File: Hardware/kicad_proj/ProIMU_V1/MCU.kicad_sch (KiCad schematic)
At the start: 8 parts, among them U9 STM32F412CEU6

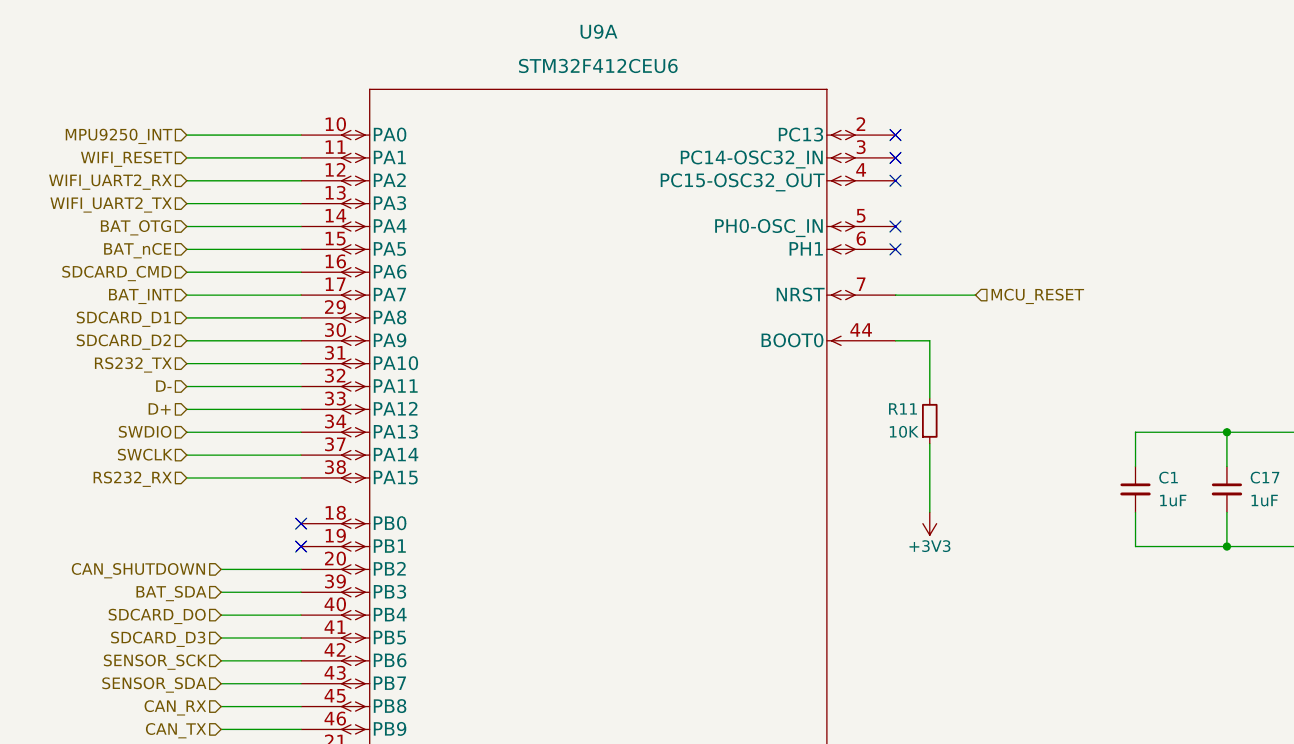
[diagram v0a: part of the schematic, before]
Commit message: Updated Schematic and Layout. Connectors and SD Card Port changed.
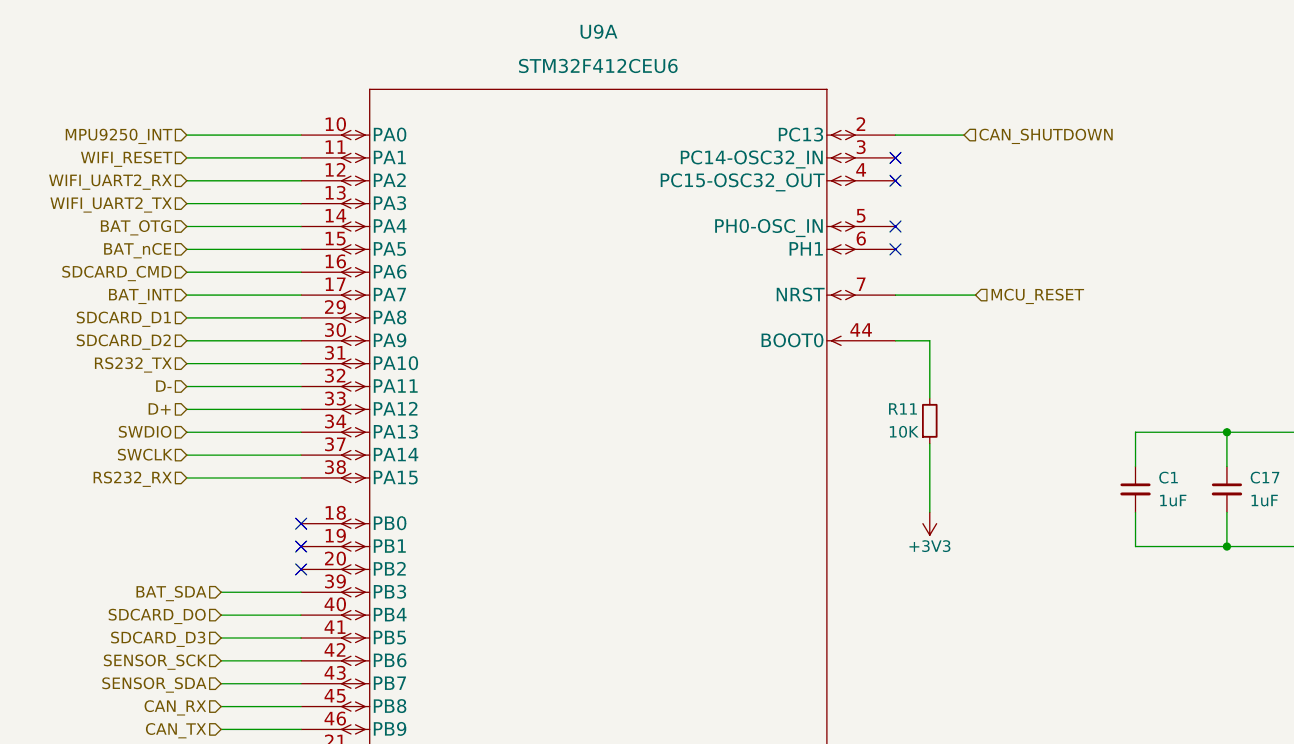
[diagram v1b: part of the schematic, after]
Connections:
- net CAN_SHUTDOWN: now also U9.2 (PC13); no longer U9.20 (PB2)
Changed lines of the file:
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@@
   (no_connect (at 175.26 39.37))
   (no_connect (at 175.26 31.75))
-  (no_connect (at 175.26 26.67))
   (no_connect (at 175.26 36.83))
   (no_connect (at 175.26 29.21))
+  (no_connect (at 109.22 74.93))
+  (no_connect (at 109.22 102.87))
+  (no_connect (at 109.22 69.85))
   (no_connect (at 109.22 72.39))
-  (no_connect (at 109.22 69.85))
-  (no_connect (at 109.22 102.87))
   (wire (pts (xy 201.93 59.69) (xy 212.09 59.69))
     (stroke (width 0) (type default) (color 0 0 0 0))
@@
     (stroke (width 0) (type default) (color 0 0 0 0))
   )
+  (wire (pts (xy 175.26 26.67) (xy 182.88 26.67))
+    (stroke (width 0) (type default) (color 0 0 0 0))
+  )
   (wire (pts (xy 100.33 77.47) (xy 109.22 77.47))
     (stroke (width 0) (type default) (color 0 0 0 0))
@@
   )
   (wire (pts (xy 201.93 72.39) (xy 212.09 72.39))
-    (stroke (width 0) (type default) (color 0 0 0 0))
-  )
-  (wire (pts (xy 100.33 74.93) (xy 109.22 74.93))
     (stroke (width 0) (type default) (color 0 0 0 0))
   )
@@
     (effects (font (size 1.27 1.27)) (justify right))
   )
-  (hierarchical_label "CAN_SHUTDOWN" (shape input) (at 100.33 74.93 180)
-    (effects (font (size 1.27 1.27)) (justify right))
+  (hierarchical_label "CAN_SHUTDOWN" (shape input) (at 182.88 26.67 0)
+    (effects (font (size 1.27 1.27)) (justify left))
   )
   (hierarchical_label "BAT_INT" (shape input) (at 96.52 44.45 180)

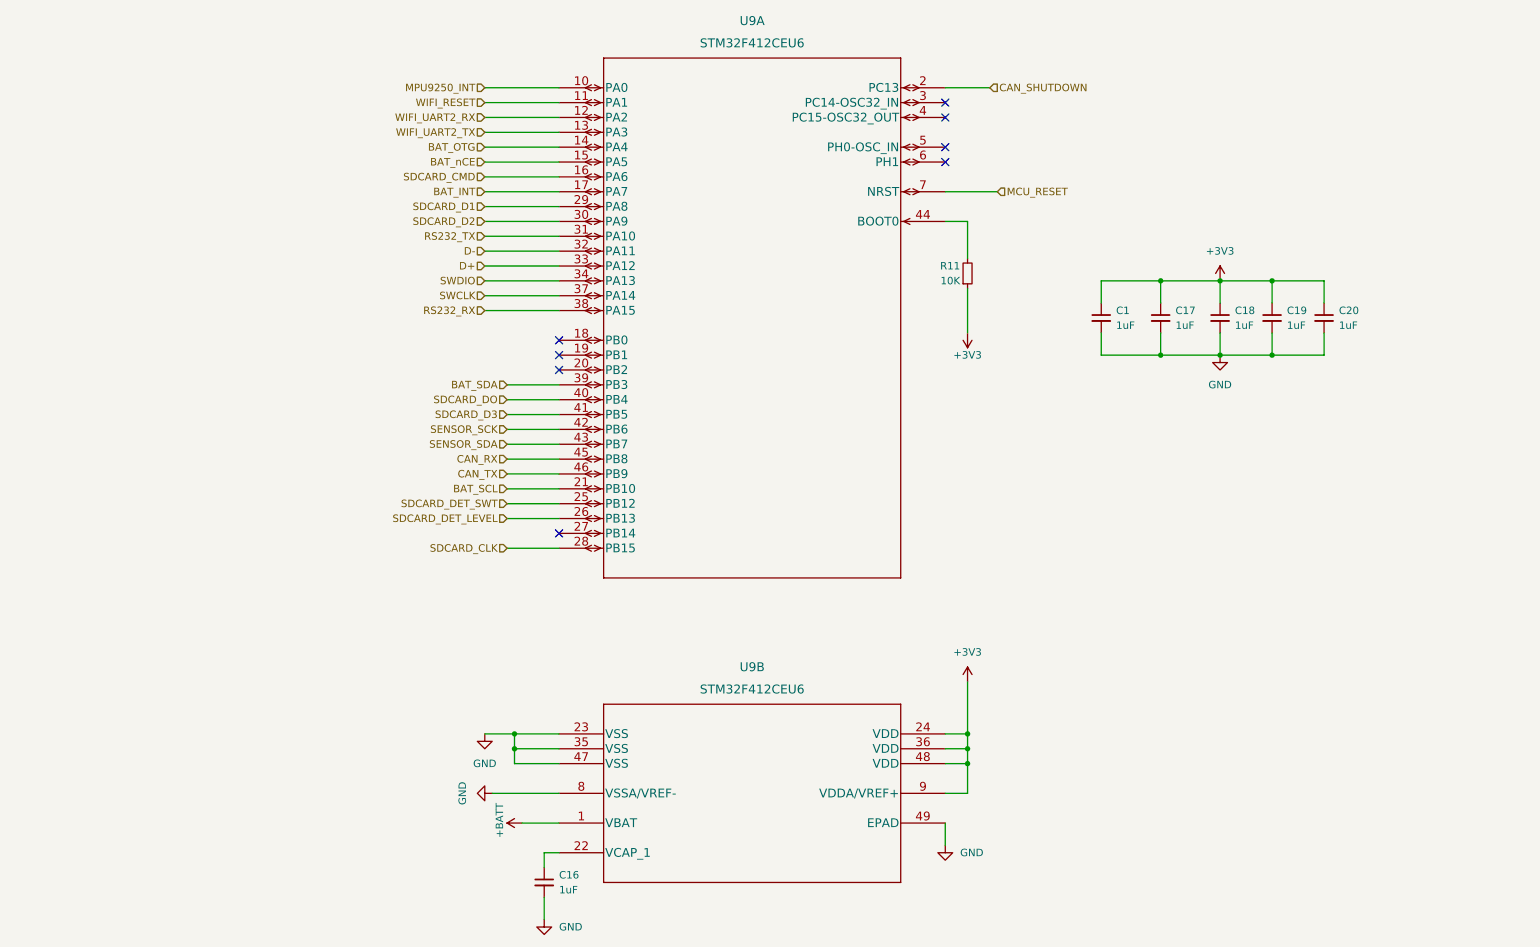
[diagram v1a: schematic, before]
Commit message: Updated schematic, layout and footprints
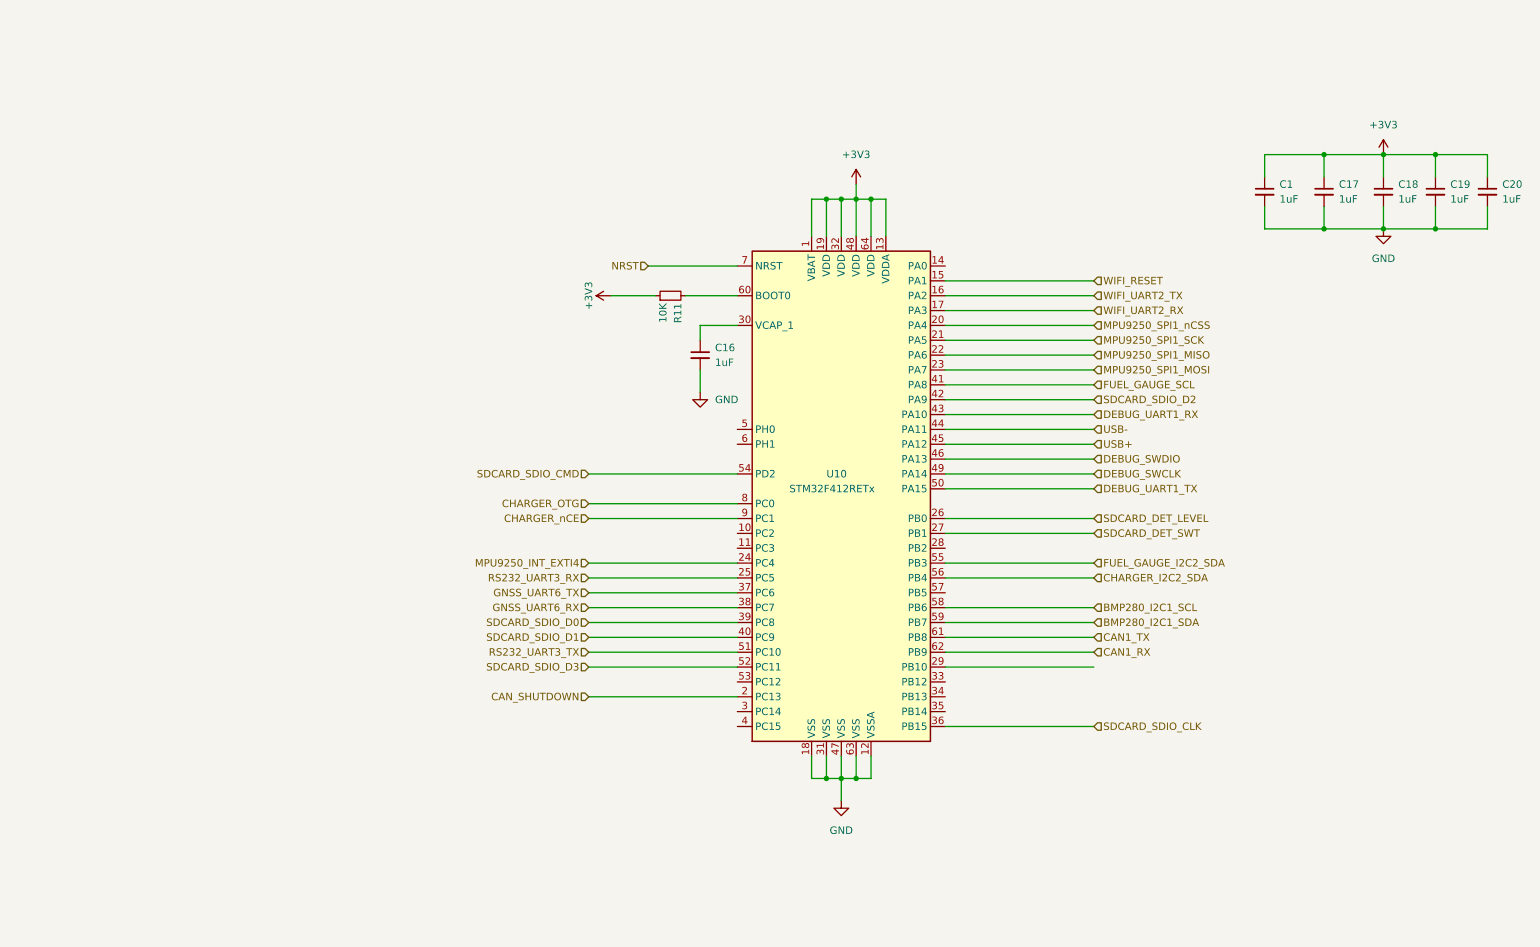
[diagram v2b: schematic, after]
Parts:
- removed U9: STM32F412CEU6, footprints:QFN50P700X700X60-49N, symbol 2022-02-05_19-28-45:STM32F412CEU6
- added U10: STM32F412RETx, Package_QFP:LQFP-64_10x10mm_P0.5mm, symbol MCU_ST_STM32F4:STM32F412RETx
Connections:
- net +3V3: now also U10.1 (VBAT), U10.13 (VDDA), U10.19 (VDD), U10.32 (VDD), U10.48 (VDD), U10.64 (VDD)
- net CAN_SHUTDOWN: now also U10.2 (PC13)
- net GND: now also U10.12 (VSSA), U10.18 (VSS), U10.31 (VSS), U10.47 (VSS), U10.63 (VSS)
- net SDCARD_DET_LEVEL: now also U10.26 (PB0)
- net SDCARD_DET_SWT: now also U10.27 (PB1)
- net WIFI_RESET: now also U10.15 (PA1)
- net WIFI_UART2_RX: now also U10.17 (PA3)
- net WIFI_UART2_TX: now also U10.16 (PA2)
- net at C16.1: now also U10.30 (VCAP_1)
- net at R11.2: now also U10.60 (BOOT0)
- new net BMP280_I2C1_SCL: U10.58 (PB6)
- new net BMP280_I2C1_SDA: U10.59 (PB7)
- new net CAN1_RX: U10.62 (PB9)
- new net CAN1_TX: U10.61 (PB8)
- new net CHARGER_I2C2_SDA: U10.56 (PB4)
- new net CHARGER_OTG: U10.8 (PC0)
- new net CHARGER_nCE: U10.9 (PC1)
- new net DEBUG_SWCLK: U10.49 (PA14)
- new net DEBUG_SWDIO: U10.46 (PA13)
- new net DEBUG_UART1_RX: U10.43 (PA10)
- new net DEBUG_UART1_TX: U10.50 (PA15)
- new net FUEL_GAUGE_I2C2_SDA: U10.55 (PB3)
- new net FUEL_GAUGE_SCL: U10.41 (PA8)
- new net GNSS_UART6_RX: U10.38 (PC7)
- new net GNSS_UART6_TX: U10.37 (PC6)
- new net MPU9250_INT_EXTI4: U10.24 (PC4)
- new net MPU9250_SPI1_MISO: U10.22 (PA6)
- new net MPU9250_SPI1_MOSI: U10.23 (PA7)
- new net MPU9250_SPI1_SCK: U10.21 (PA5)
- new net MPU9250_SPI1_nCSS: U10.20 (PA4)
- new net NRST: U10.7 (NRST)
- new net RS232_UART3_RX: U10.25 (PC5)
- new net RS232_UART3_TX: U10.51 (PC10)
- new net SDCARD_SDIO_CLK: U10.36 (PB15)
- new net SDCARD_SDIO_CMD: U10.54 (PD2)
- new net SDCARD_SDIO_D0: U10.39 (PC8)
- new net SDCARD_SDIO_D1: U10.40 (PC9)
- new net SDCARD_SDIO_D2: U10.42 (PA9)
- new net SDCARD_SDIO_D3: U10.52 (PC11)
- new net USB+: U10.45 (PA12)
- new net USB-: U10.44 (PA11)
- no-connect marks 8 -> 0
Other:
- moved on the sheet: C1, C16, C17, C18, C19, C20, R11

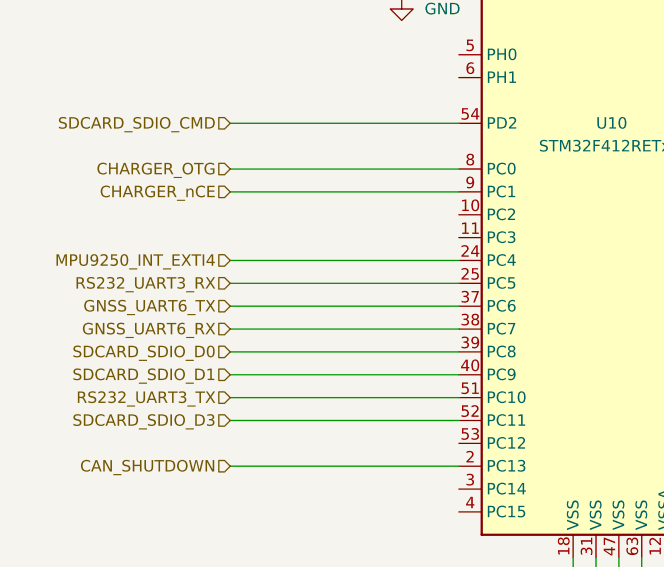
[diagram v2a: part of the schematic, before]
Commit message: Updated Layout, schematic, added new symbol and footprint
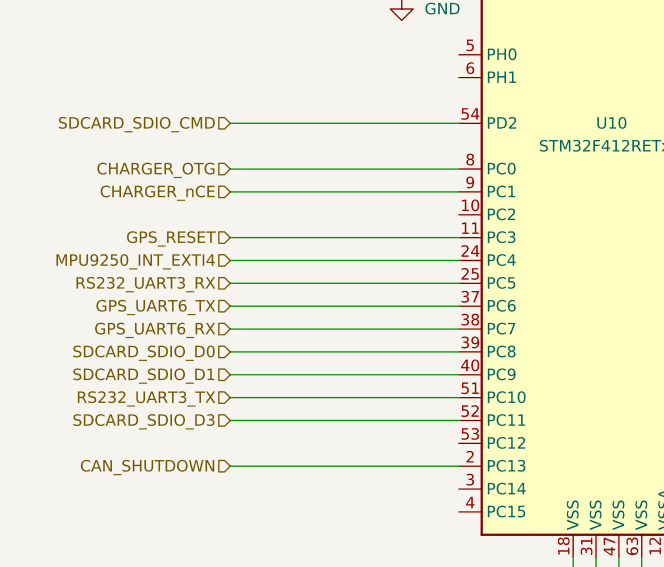
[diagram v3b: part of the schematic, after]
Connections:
- net GPS_RESET: now reaches U10.11 (PC3)
- net GNSS_UART6_RX renamed GPS_UART6_RX
- net GNSS_UART6_TX renamed GPS_UART6_TX
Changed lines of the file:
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@@
+    (stroke (width 0) (type default) (color 0 0 0 0))
+  )
+  (wire (pts (xy 114.3 105.41) (xy 139.7 105.41))
     (stroke (width 0) (type default) (color 0 0 0 0))
   )
@@
     (stroke (width 0) (type default) (color 0 0 0 0))
   )
-  (hierarchical_label "GNSS_UART6_TX" (shape input) (at 114.3 113.03 180)
+  (hierarchical_label "GPS_UART6_TX" (shape input) (at 114.3 113.03 180)
     (effects (font (size 1.27 1.27)) (justify right))
   )
@@
     (effects (font (size 1.27 1.27)) (justify left))
   )
+  (hierarchical_label "GPS_RESET" (shape input) (at 114.3 105.41 180)
+    (effects (font (size 1.27 1.27)) (justify right))
+  )
   (hierarchical_label "MPU9250_SPI1_MOSI" (shape input) (at 200.66 74.93 0)
     (effects (font (size 1.27 1.27)) (justify left))
@@
     (effects (font (size 1.27 1.27)) (justify left))
   )
-  (hierarchical_label "GNSS_UART6_RX" (shape input) (at 114.3 115.57 180)
-    (effects (font (size 1.27 1.27)) (justify right))
-  )
+  (hierarchical_label "GPS_UART6_RX" (shape input) (at 114.3 115.57 180)
+    (effects (font (size 1.27 1.27)) (justify right))
+  )

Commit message: Updated Schematic and Layout
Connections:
- net GPS_RESET: now also U10.28 (PB2); no longer U10.11 (PC3)
- no-connect marks 0 -> 1
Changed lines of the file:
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@@
   (junction (at 240.03 38.1) (diameter 0) (color 0 0 0 0)
   )
+  (no_connect (at 139.7 105.41))
   (wire (pts (xy 229.87 38.1) (xy 240.03 38.1))
     (stroke (width 0) (type default) (color 0 0 0 0))
@@
     (stroke (width 0) (type default) (color 0 0 0 0))
   )
+  (wire (pts (xy 175.26 105.41) (xy 200.66 105.41))
+    (stroke (width 0) (type default) (color 0 0 0 0))
+  )
   (wire (pts (xy 162.56 144.78) (xy 162.56 140.97))
     (stroke (width 0) (type default) (color 0 0 0 0))
   )
-  (wire (pts (xy 114.3 105.41) (xy 139.7 105.41))
-    (stroke (width 0) (type default) (color 0 0 0 0))
-  )
   (wire (pts (xy 175.26 92.71) (xy 200.66 92.71))
     (stroke (width 0) (type default) (color 0 0 0 0))
@@
   )
   (wire (pts (xy 175.26 107.95) (xy 200.66 107.95))
-    (stroke (width 0) (type default) (color 0 0 0 0))
-  )
-  (wire (pts (xy 175.26 125.73) (xy 200.66 125.73))
     (stroke (width 0) (type default) (color 0 0 0 0))
   )
@@
     (effects (font (size 1.27 1.27)) (justify left))
   )
-  (hierarchical_label "GPS_RESET" (shape input) (at 114.3 105.41 180)
-    (effects (font (size 1.27 1.27)) (justify right))
+  (hierarchical_label "GPS_RESET" (shape input) (at 200.66 105.41 0)
+    (effects (font (size 1.27 1.27)) (justify left))
   )
   (hierarchical_label "MPU9250_SPI1_MOSI" (shape input) (at 200.66 74.93 0)

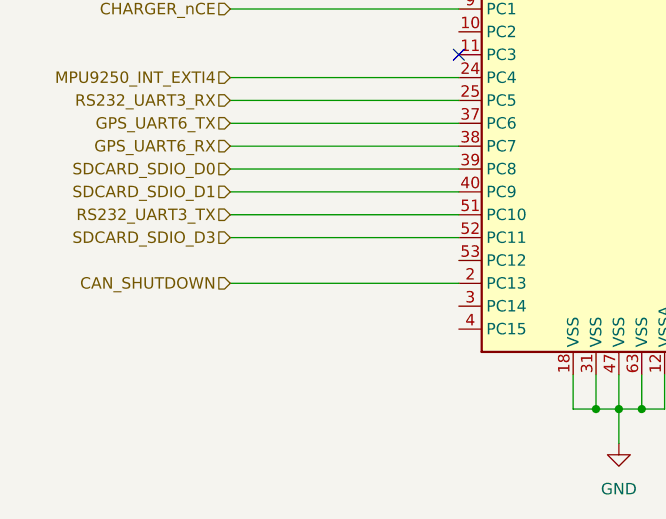
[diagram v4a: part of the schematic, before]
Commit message: Updated layout
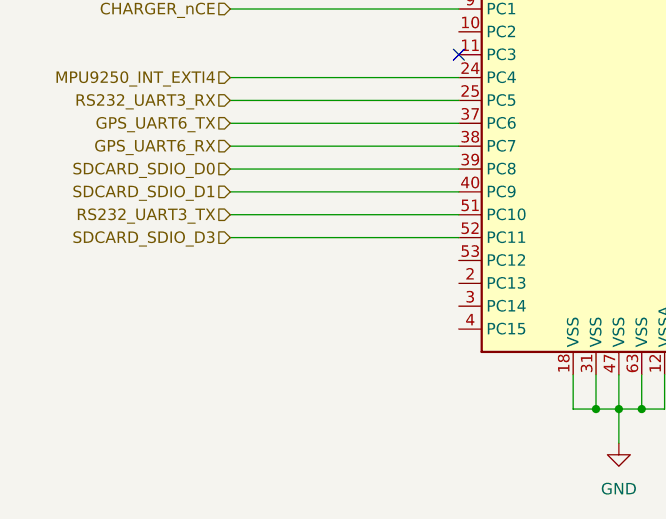
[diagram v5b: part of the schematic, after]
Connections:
- net CAN_SHUTDOWN: no longer names the net of U10.2 (PC13)
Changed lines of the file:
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@@
-    (stroke (width 0) (type default) (color 0 0 0 0))
-  )
-  (wire (pts (xy 114.3 130.81) (xy 139.7 130.81))
     (stroke (width 0) (type default) (color 0 0 0 0))
   )
@@
     (effects (font (size 1.27 1.27)) (justify left))
   )
-  (hierarchical_label "CAN_SHUTDOWN" (shape input) (at 114.3 130.81 180)
-    (effects (font (size 1.27 1.27)) (justify right))
-  )
   (hierarchical_label "DEBUG_SWDIO" (shape input) (at 200.66 90.17 0)
